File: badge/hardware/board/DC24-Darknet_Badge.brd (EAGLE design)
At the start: 101.6 x 83.8 mm, 54 parts, among them Q1 SOP22, SW0 SWITCH_TACTILETACTILE-2PIN-NA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, SW1 SWITCH_TACTILETACTILE-2PIN-NA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, SW2 SWITCH_TACTILETACTILE-2PIN-NA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, SW3 SWITCH_TACTILETACTILE-2PIN-NA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, SW4 SWITCH_TACTILETACTILE-2PIN-NA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, SW5 SWITCH_TACTILETACTILE-2PIN-NA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, SW6 SWITCH_TACTILETACTILE-2PIN-NA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, SW7 SWITCH_TACTILETACTILE-2PIN-NA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, SW8 SWITCH_TACTILETACTILE-2PIN-NA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

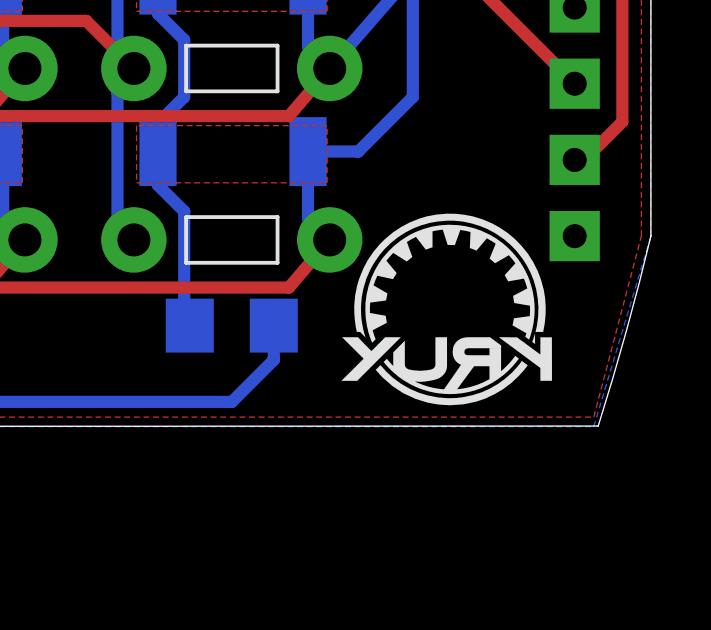
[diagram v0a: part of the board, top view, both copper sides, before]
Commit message: moved board files over so we don't lose them
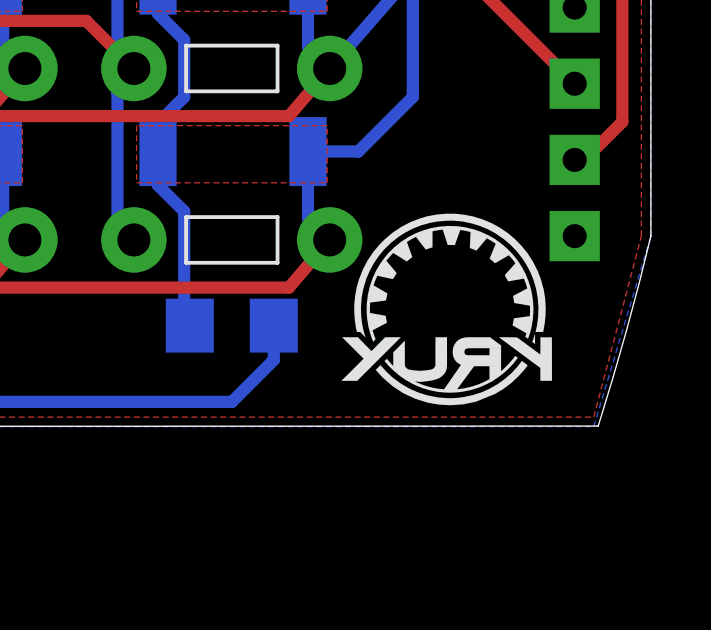
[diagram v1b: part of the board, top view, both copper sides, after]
